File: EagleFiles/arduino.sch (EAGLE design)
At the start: 21 parts, among them IC2 74250N, IC3 74250N, IC4 74250N, U1 ATMEGA168

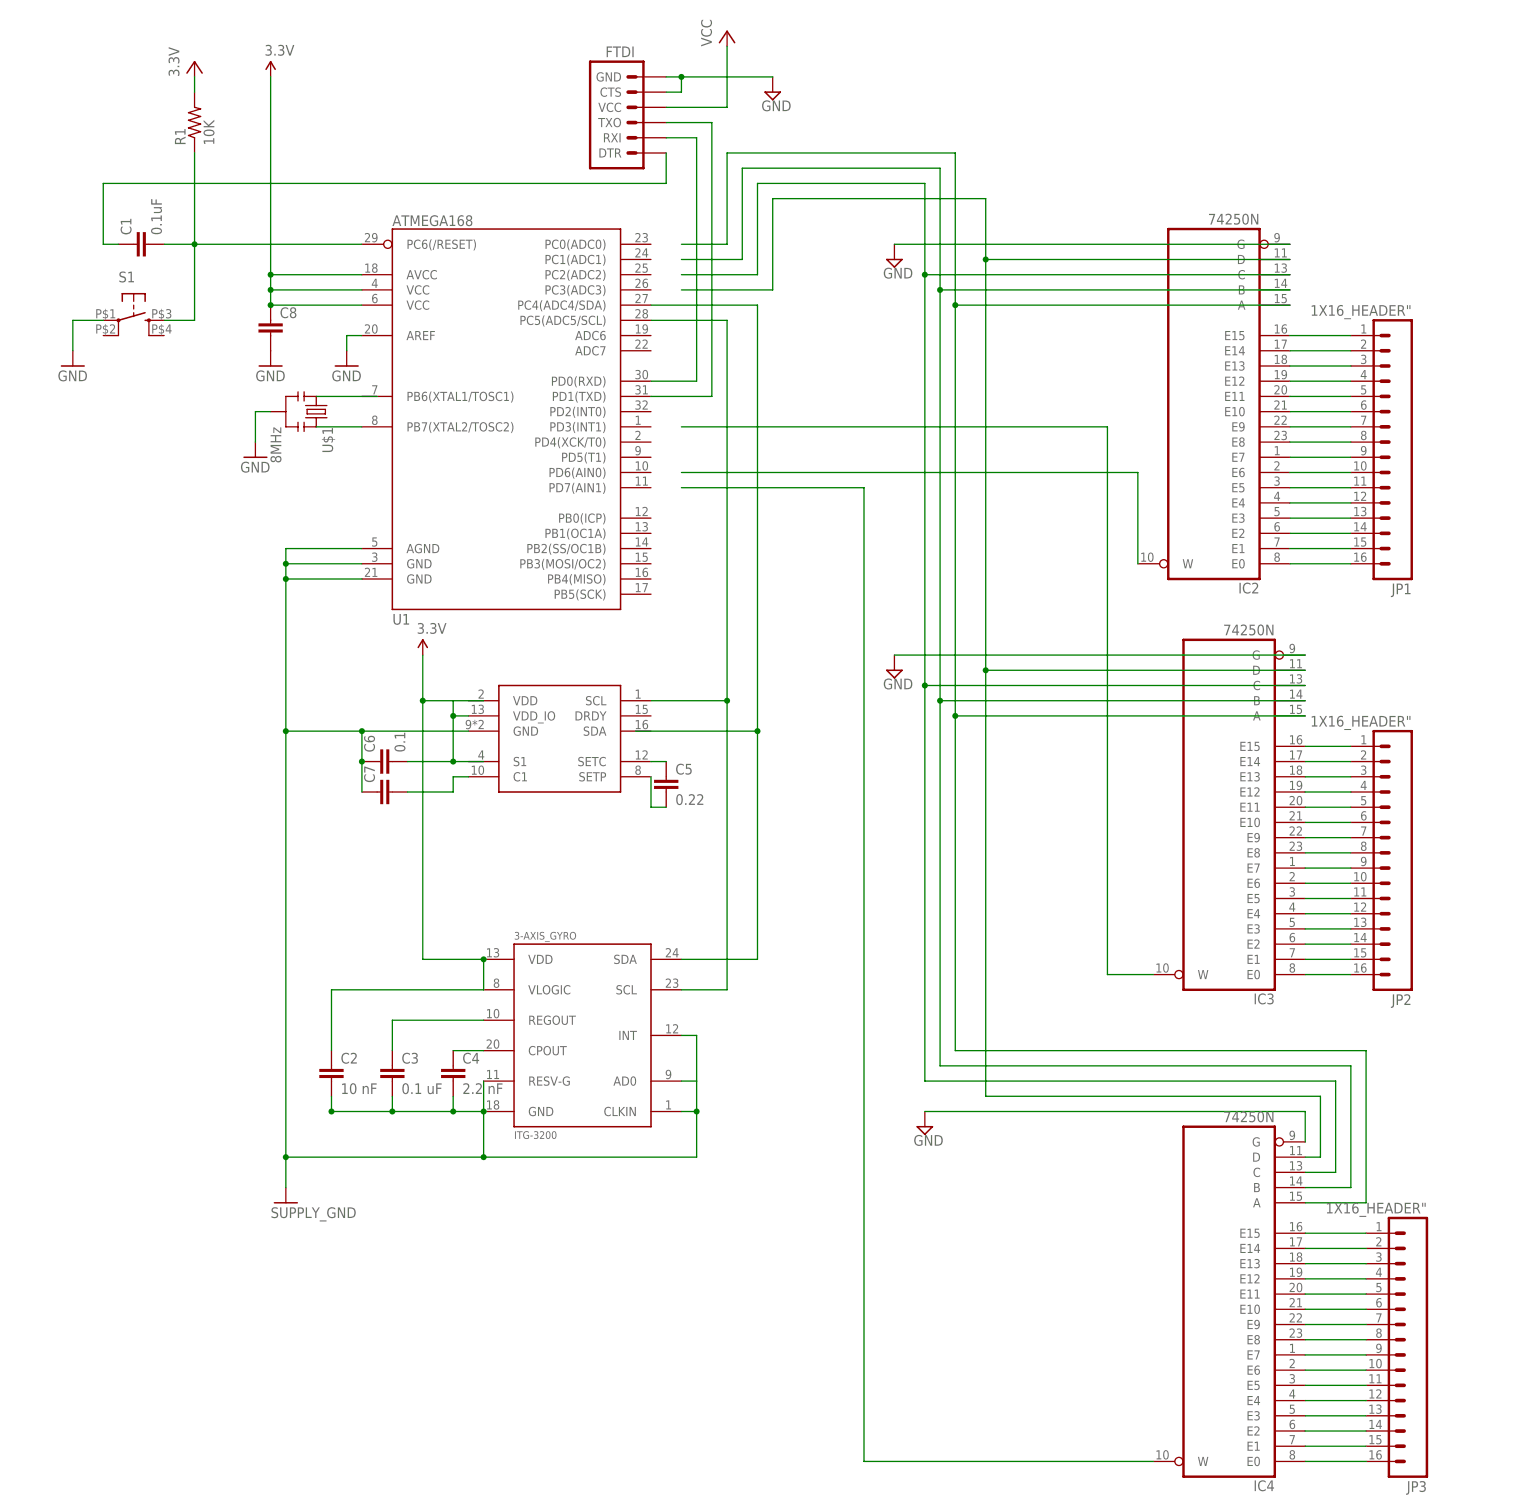
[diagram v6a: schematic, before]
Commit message: added connections for muxs
hopefully in the right spot this time...
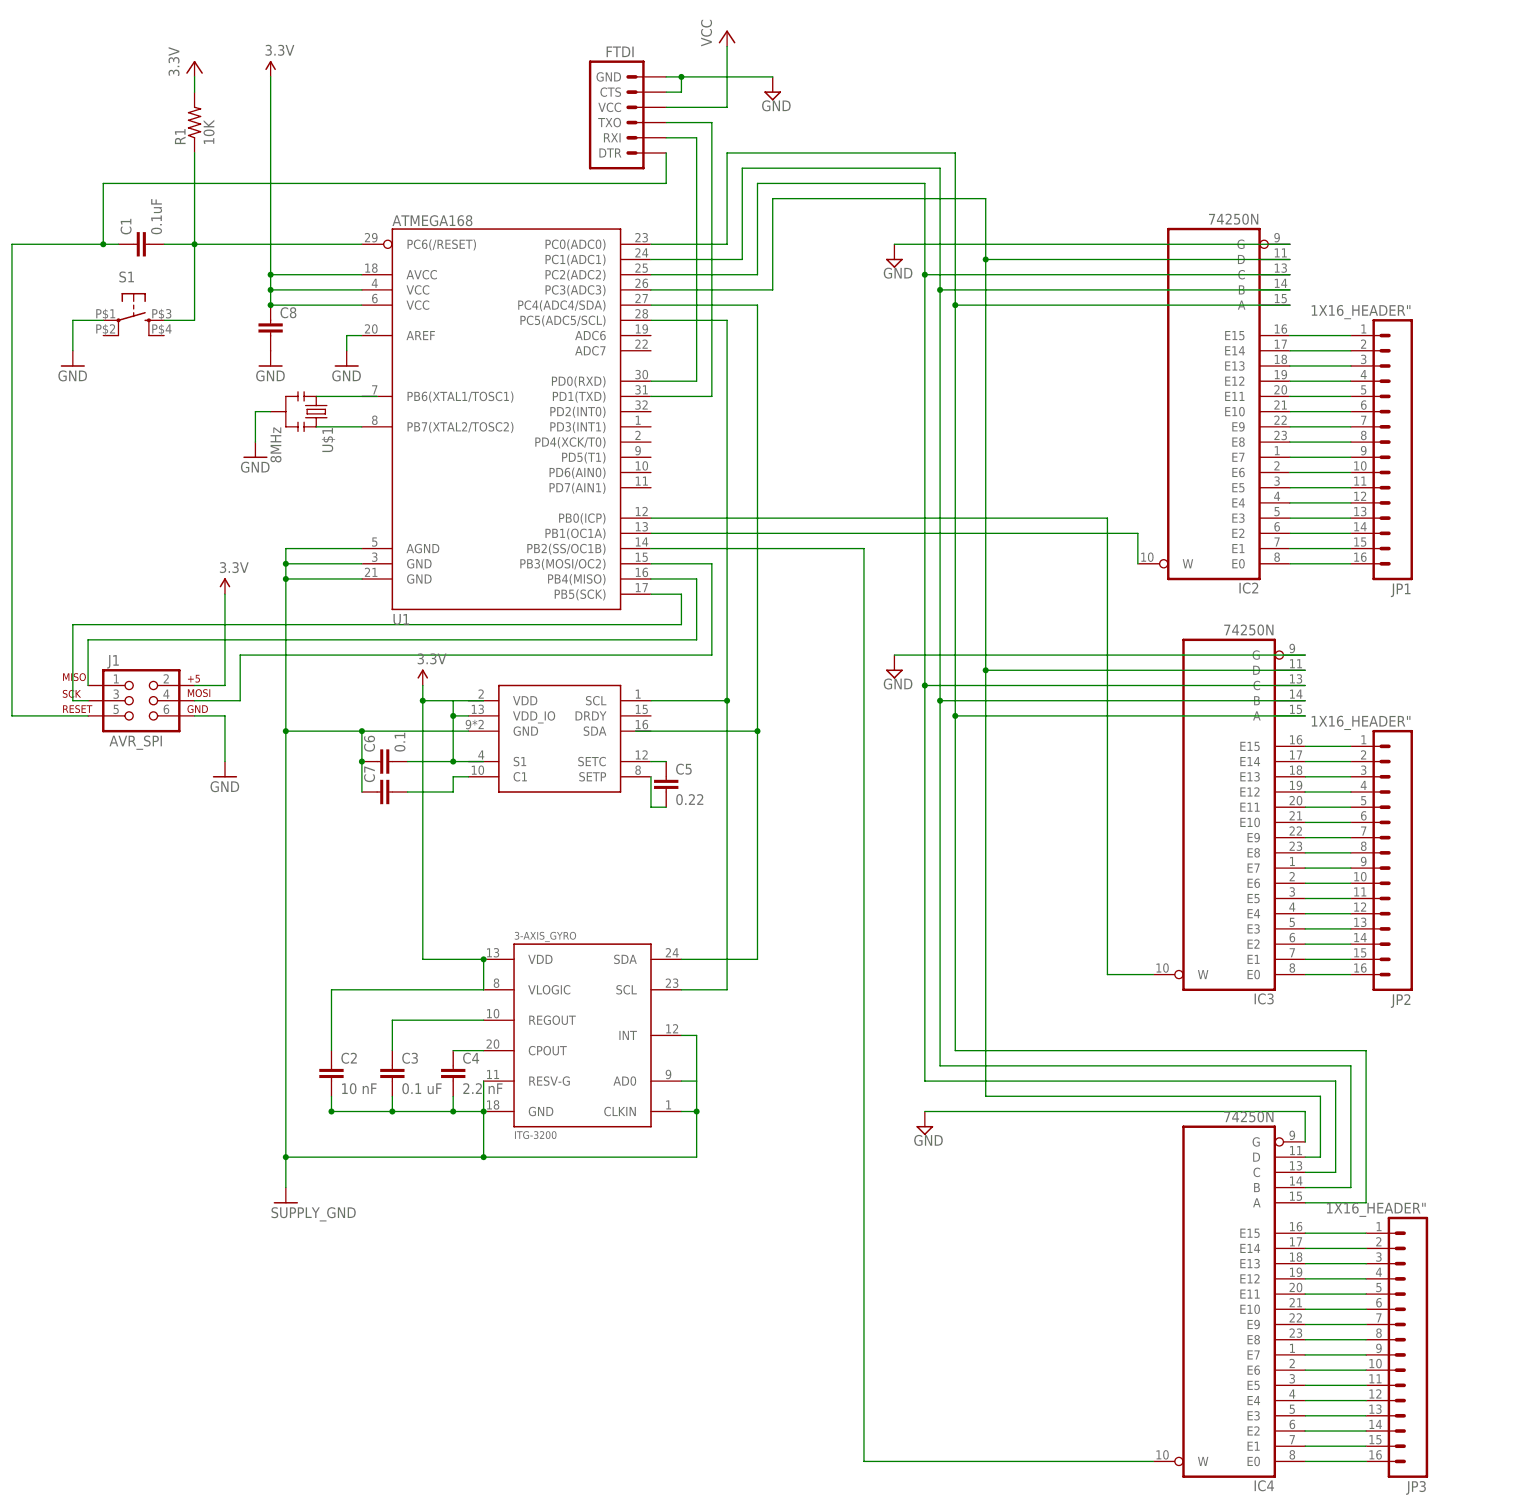
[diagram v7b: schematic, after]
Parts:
- added J1: AVR_SPI, SparkFun:AVR_SPI_PRG_6PTH
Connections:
- new net N$67: J1.1, U1.PB4(MISO)
- new net N$68: J1.3, U1.PB5(SCK)
- new net N$71: J1.4, U1.PB3(MOSI/OC2)
- net GND: now also J1.6
- net N$2: now also U1.PC2(ADC2)
- net N$3: now also U1.PC1(ADC1)
- net N$39: now also J1.5
- net N$4: now also U1.PC0(ADC0)
- net N$42: now also U1.PB2(SS/OC1B)
- net N$5: now also U1.PB1(OC1A)
- net N$6: now also U1.PB0(ICP)
- net N$7: now also U1.PC3(ADC3)
- net VCC: now also J1.2
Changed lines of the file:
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@@
 <part name="C8" library="SparkFun" deviceset="CAP" device="0603-CAP"/>
 <part name="GND5" library="supply1" deviceset="GND" device=""/>
+<part name="J1" library="SparkFun" deviceset="AVR_SPI_PRG_6" device="PTH" value="AVR_SPI"/>
+<part name="GND6" library="supply1" deviceset="GND" device=""/>
+<part name="P+5" library="SparkFun" deviceset="VCC" device="" value="3.3V"/>
 </parts>
 <sheets>
@@
 <instance part="P+1" gate="VCC" x="127" y="134.62"/>
 <instance part="U1" gate="G$1" x="88.9" y="73.66"/>
-<instance part="P+3" gate="1" x="76.2" y="30.48"/>
+<instance part="P+3" gate="1" x="76.2" y="25.4"/>
 <instance part="P+2" gate="1" x="50.8" y="127"/>
 <instance part="C1" gate="G$1" x="30.48" y="99.06" rot="R90"/>
@@
 <instance part="C8" gate="G$1" x="50.8" y="83.82"/>
 <instance part="GND5" gate="1" x="50.8" y="78.74"/>
+<instance part="J1" gate="G$1" x="27.94" y="22.86"/>
+<instance part="GND6" gate="1" x="43.18" y="10.16"/>
+<instance part="P+5" gate="1" x="43.18" y="40.64"/>
 </instances>
 <busses>
@@
 <pinref part="GND5" gate="1" pin="GND"/>
 </segment>
+<segment>
+<pinref part="J1" gate="G$1" pin="6"/>
+<wire x1="38.1" y1="20.32" x2="43.18" y2="20.32" width="0.1524" layer="91"/>
+<wire x1="43.18" y1="20.32" x2="43.18" y2="12.7" width="0.1524" layer="91"/>
+<pinref part="GND6" gate="1" pin="GND"/>
+</segment>
 </net>
 <net name="N$2" class="0">
@@
 <wire x1="160.02" y1="93.98" x2="160.02" y2="109.22" width="0.1524" layer="91"/>
 <wire x1="160.02" y1="109.22" x2="132.08" y2="109.22" width="0.1524" layer="91"/>
-<wire x1="119.38" y1="93.98" x2="132.08" y2="93.98" width="0.1524" layer="91"/>
+<wire x1="114.3" y1="93.98" x2="132.08" y2="93.98" width="0.1524" layer="91"/>
 <wire x1="132.08" y1="93.98" x2="132.08" y2="109.22" width="0.1524" layer="91"/>
 <wire x1="160.02" y1="93.98" x2="160.02" y2="25.4" width="0.1524" layer="91"/>
@@
 <wire x1="160.02" y1="-40.64" x2="160.02" y2="25.4" width="0.1524" layer="91"/>
 <junction x="160.02" y="25.4"/>
+<pinref part="U1" gate="G$1" pin="PC2(ADC2)"/>
 </segment>
 </net>
@@
 <wire x1="162.56" y1="91.44" x2="162.56" y2="111.76" width="0.1524" layer="91"/>
 <wire x1="162.56" y1="111.76" x2="129.54" y2="111.76" width="0.1524" layer="91"/>
-<wire x1="119.38" y1="96.52" x2="129.54" y2="96.52" width="0.1524" layer="91"/>
+<wire x1="114.3" y1="96.52" x2="129.54" y2="96.52" width="0.1524" layer="91"/>
 <wire x1="129.54" y1="96.52" x2="129.54" y2="111.76" width="0.1524" layer="91"/>
 <wire x1="162.56" y1="91.44" x2="162.56" y2="22.86" width="0.1524" layer="91"/>
@@
 <wire x1="162.56" y1="-38.1" x2="162.56" y2="22.86" width="0.1524" layer="91"/>
 <junction x="162.56" y="22.86"/>
+<pinref part="U1" gate="G$1" pin="PC1(ADC1)"/>
 </segment>
 </net>
@@
 <wire x1="165.1" y1="88.9" x2="165.1" y2="114.3" width="0.1524" layer="91"/>
 <wire x1="165.1" y1="114.3" x2="127" y2="114.3" width="0.1524" layer="91"/>
-<wire x1="119.38" y1="99.06" x2="127" y2="99.06" width="0.1524" layer="91"/>
+<wire x1="114.3" y1="99.06" x2="127" y2="99.06" width="0.1524" layer="91"/>
 <wire x1="127" y1="99.06" x2="127" y2="114.3" width="0.1524" layer="91"/>
 <wire x1="165.1" y1="88.9" x2="165.1" y2="20.32" width="0.1524" layer="91"/>
@@
 <wire x1="165.1" y1="-35.56" x2="165.1" y2="20.32" width="0.1524" layer="91"/>
 <junction x="165.1" y="20.32"/>
+<pinref part="U1" gate="G$1" pin="PC0(ADC0)"/>
 </segment>
 </net>
@@
 <segment>
 <pinref part="IC2" gate="A" pin="W"/>
-<wire x1="195.58" y1="45.72" x2="195.58" y2="60.96" width="0.1524" layer="91"/>
-<wire x1="119.38" y1="60.96" x2="195.58" y2="60.96" width="0.1524" layer="91"/>
+<wire x1="195.58" y1="45.72" x2="195.58" y2="50.8" width="0.1524" layer="91"/>
+<wire x1="114.3" y1="50.8" x2="195.58" y2="50.8" width="0.1524" layer="91"/>
+<pinref part="U1" gate="G$1" pin="PB1(OC1A)"/>
 </segment>
 </net>
@@
 <pinref part="IC3" gate="A" pin="W"/>
 <wire x1="198.12" y1="-22.86" x2="190.5" y2="-22.86" width="0.1524" layer="91"/>
-<wire x1="190.5" y1="-22.86" x2="190.5" y2="68.58" width="0.1524" layer="91"/>
-<wire x1="119.38" y1="68.58" x2="190.5" y2="68.58" width="0.1524" layer="91"/>
+<wire x1="190.5" y1="-22.86" x2="190.5" y2="53.34" width="0.1524" layer="91"/>
+<wire x1="114.3" y1="53.34" x2="190.5" y2="53.34" width="0.1524" layer="91"/>
+<pinref part="U1" gate="G$1" pin="PB0(ICP)"/>
 </segment>
 </net>
@@
 <wire x1="170.18" y1="-43.18" x2="170.18" y2="27.94" width="0.1524" layer="91"/>
 <junction x="170.18" y="27.94"/>
-<wire x1="119.38" y1="91.44" x2="134.62" y2="91.44" width="0.1524" layer="91"/>
+<wire x1="114.3" y1="91.44" x2="134.62" y2="91.44" width="0.1524" layer="91"/>
+<pinref part="U1" gate="G$1" pin="PC3(ADC3)"/>
 </segment>
 </net>
@@
 <pinref part="IC4" gate="A" pin="W"/>
 <wire x1="198.12" y1="-104.14" x2="149.86" y2="-104.14" width="0.1524" layer="91"/>
-<wire x1="149.86" y1="-104.14" x2="149.86" y2="58.42" width="0.1524" layer="91"/>
-<wire x1="119.38" y1="58.42" x2="149.86" y2="58.42" width="0.1524" layer="91"/>
+<wire x1="149.86" y1="-104.14" x2="149.86" y2="48.26" width="0.1524" layer="91"/>
+<wire x1="114.3" y1="48.26" x2="149.86" y2="48.26" width="0.1524" layer="91"/>
+<pinref part="U1" gate="G$1" pin="PB2(SS/OC1B)"/>
 </segment>
 </net>
@@
 <junction x="86.36" y="-20.32"/>
 <wire x1="86.36" y1="-20.32" x2="76.2" y2="-20.32" width="0.1524" layer="91"/>
-<wire x1="76.2" y1="30.48" x2="76.2" y2="22.86" width="0.1524" layer="91"/>
+<wire x1="76.2" y1="25.4" x2="76.2" y2="22.86" width="0.1524" layer="91"/>
 <pinref part="P+3" gate="1" pin="VCC"/>
 <wire x1="76.2" y1="22.86" x2="76.2" y2="-20.32" width="0.1524" layer="91"/>
@@
 <wire x1="38.1" y1="127" x2="38.1" y2="124.46" width="0.1524" layer="91"/>
 </segment>
+<segment>
+<pinref part="J1" gate="G$1" pin="2"/>
+<wire x1="38.1" y1="25.4" x2="43.18" y2="25.4" width="0.1524" layer="91"/>
+<wire x1="43.18" y1="25.4" x2="43.18" y2="40.64" width="0.1524" layer="91"/>
+<pinref part="P+5" gate="1" pin="VCC"/>
+</segment>
 </net>
 <net name="N$39" class="0">
@@
 <pinref part="C1" gate="G$1" pin="1"/>
 <wire x1="22.86" y1="99.06" x2="25.4" y2="99.06" width="0.1524" layer="91"/>
+<pinref part="J1" gate="G$1" pin="5"/>
+<wire x1="20.32" y1="20.32" x2="7.62" y2="20.32" width="0.1524" layer="91"/>
+<wire x1="7.62" y1="20.32" x2="7.62" y2="99.06" width="0.1524" layer="91"/>
+<wire x1="7.62" y1="99.06" x2="22.86" y2="99.06" width="0.1524" layer="91"/>
+<junction x="22.86" y="99.06"/>
 </segment>
 </net>
@@
 </segment>
 </net>
+<net name="N$67" class="0">
+<segment>
+<pinref part="J1" gate="G$1" pin="1"/>
+<wire x1="20.32" y1="25.4" x2="20.32" y2="33.02" width="0.1524" layer="91"/>
+<wire x1="20.32" y1="33.02" x2="121.92" y2="33.02" width="0.1524" layer="91"/>
+<pinref part="U1" gate="G$1" pin="PB4(MISO)"/>
+<wire x1="114.3" y1="43.18" x2="121.92" y2="43.18" width="0.1524" layer="91"/>
+<wire x1="121.92" y1="43.18" x2="121.92" y2="33.02" width="0.1524" layer="91"/>
+</segment>
+</net>
+<net name="N$68" class="0">
+<segment>
+<pinref part="J1" gate="G$1" pin="3"/>
+<wire x1="20.32" y1="22.86" x2="17.78" y2="22.86" width="0.1524" layer="91"/>
+<wire x1="17.78" y1="22.86" x2="17.78" y2="35.56" width="0.1524" layer="91"/>
+<wire x1="17.78" y1="35.56" x2="119.38" y2="35.56" width="0.1524" layer="91"/>
+<wire x1="119.38" y1="35.56" x2="119.38" y2="40.64" width="0.1524" layer="91"/>
+<pinref part="U1" gate="G$1" pin="PB5(SCK)"/>
+<wire x1="119.38" y1="40.64" x2="114.3" y2="40.64" width="0.1524" layer="91"/>
+</segment>
+</net>
+<net name="N$71" class="0">
+<segment>
+<pinref part="J1" gate="G$1" pin="4"/>
+<wire x1="38.1" y1="22.86" x2="45.72" y2="22.86" width="0.1524" layer="91"/>
+<wire x1="45.72" y1="22.86" x2="45.72" y2="30.48" width="0.1524" layer="91"/>
+<wire x1="45.72" y1="30.48" x2="124.46" y2="30.48" width="0.1524" layer="91"/>
+<wire x1="124.46" y1="30.48" x2="124.46" y2="45.72" width="0.1524" layer="91"/>
+<pinref part="U1" gate="G$1" pin="PB3(MOSI/OC2)"/>
+<wire x1="124.46" y1="45.72" x2="114.3" y2="45.72" width="0.1524" layer="91"/>
+</segment>
+</net>

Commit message: finished first rev
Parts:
- added JP4: OP_AMP, RBBB:1X04_HEADER"
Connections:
- removed net N$3: IC2A.B, IC3A.B, IC4A.B, U1.PC1(ADC1)
- removed net N$4: IC2A.A, IC3A.A, IC4A.A, U1.PC0(ADC0)
- new net N$72: JP4.3, U1.PB1(OC1A)
- new net N$73: JP4.1, U1.PD5(T1)
- new net N$74: JP4.2, U1.PD6(AIN0)
- new net N$75: JP4.4, U1.PB2(SS/OC1B)
- net N$2: now also U1.PD7(AIN1); no longer U1.PC2(ADC2)
- net N$42: now also U1.PD3(INT1); no longer U1.PB2(SS/OC1B)
- net N$43: no longer U1.PC4(ADC4/SDA)
- net N$5: now also U1.PD2(INT0); no longer U1.PB1(OC1A)
- net N$6: now also U1.PD4(XCK/T0); no longer U1.PB0(ICP)
- net N$63: now also IC2A.A, IC3A.A, IC4A.A
- net N$66: now also IC2A.B, IC3A.B, IC4A.B
- net N$7: now also U1.PB0(ICP); no longer U1.PC3(ADC3)
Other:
- moved on the sheet: IC2, JP1
